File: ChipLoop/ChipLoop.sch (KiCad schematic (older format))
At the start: 33 parts, among them J1 Jumper, J2 Conn_02x25_Counter_Clockwise, Q1 2N3904, SW1 SW_A, SW2 SW_B, U1 ATtiny84A-PU, U2 ISD1820P, U3 L78L05_TO92

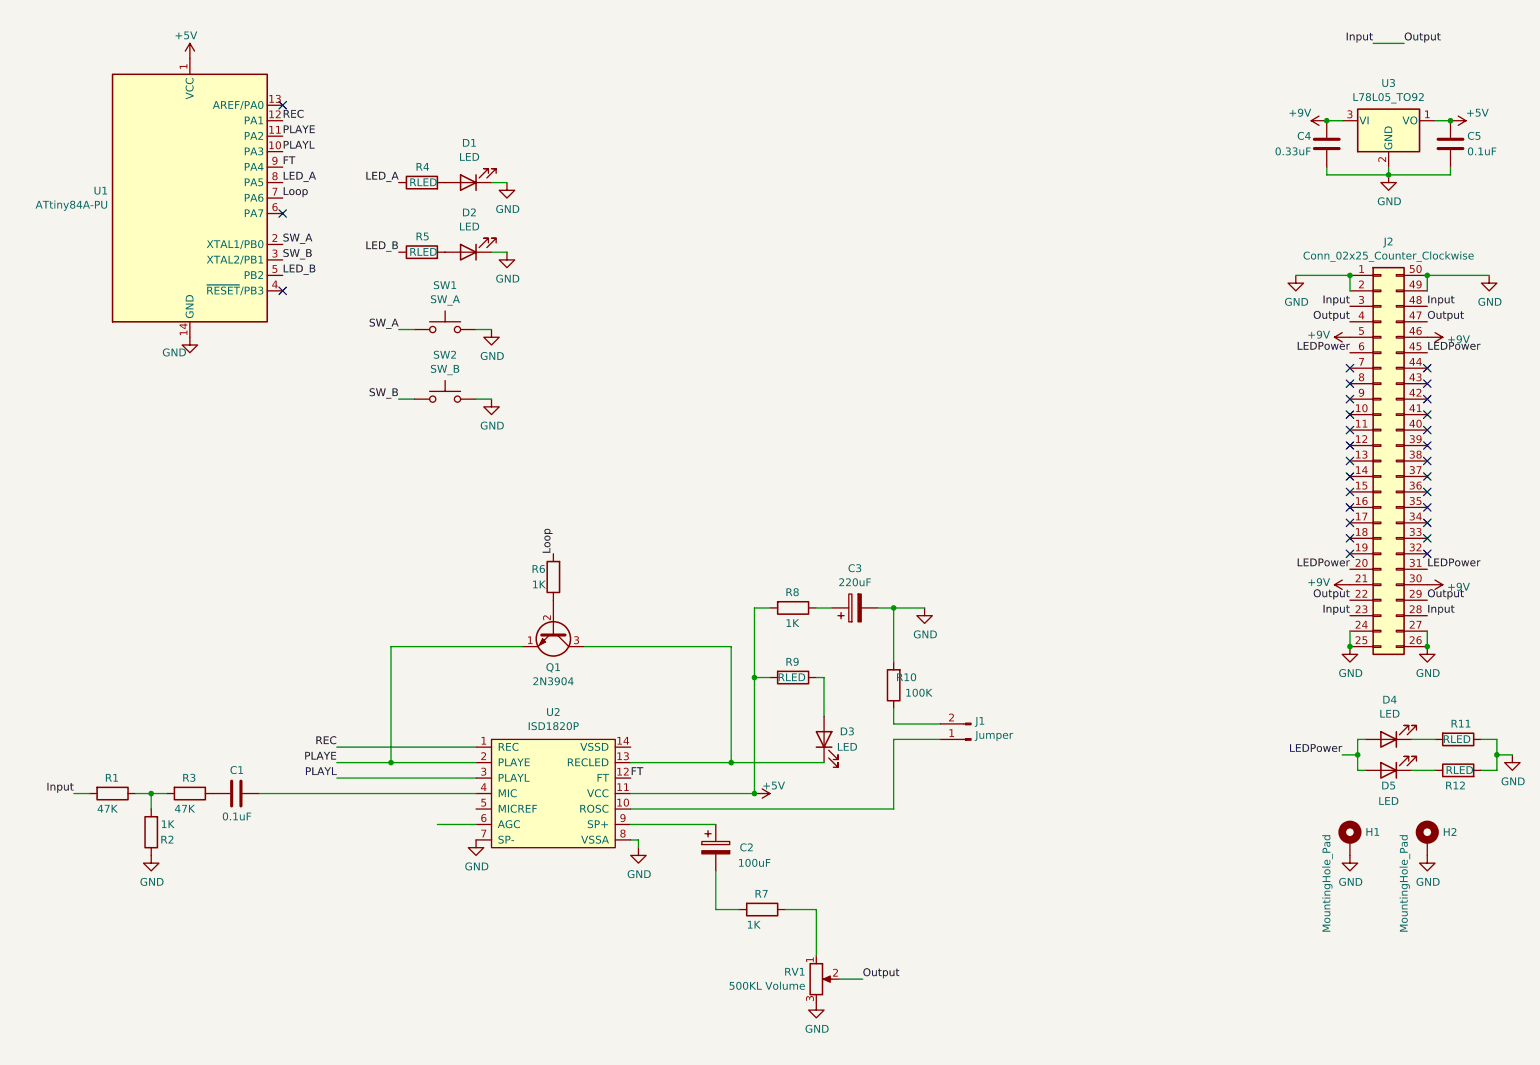
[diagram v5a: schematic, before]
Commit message: Finalized new version of ChipLoop board
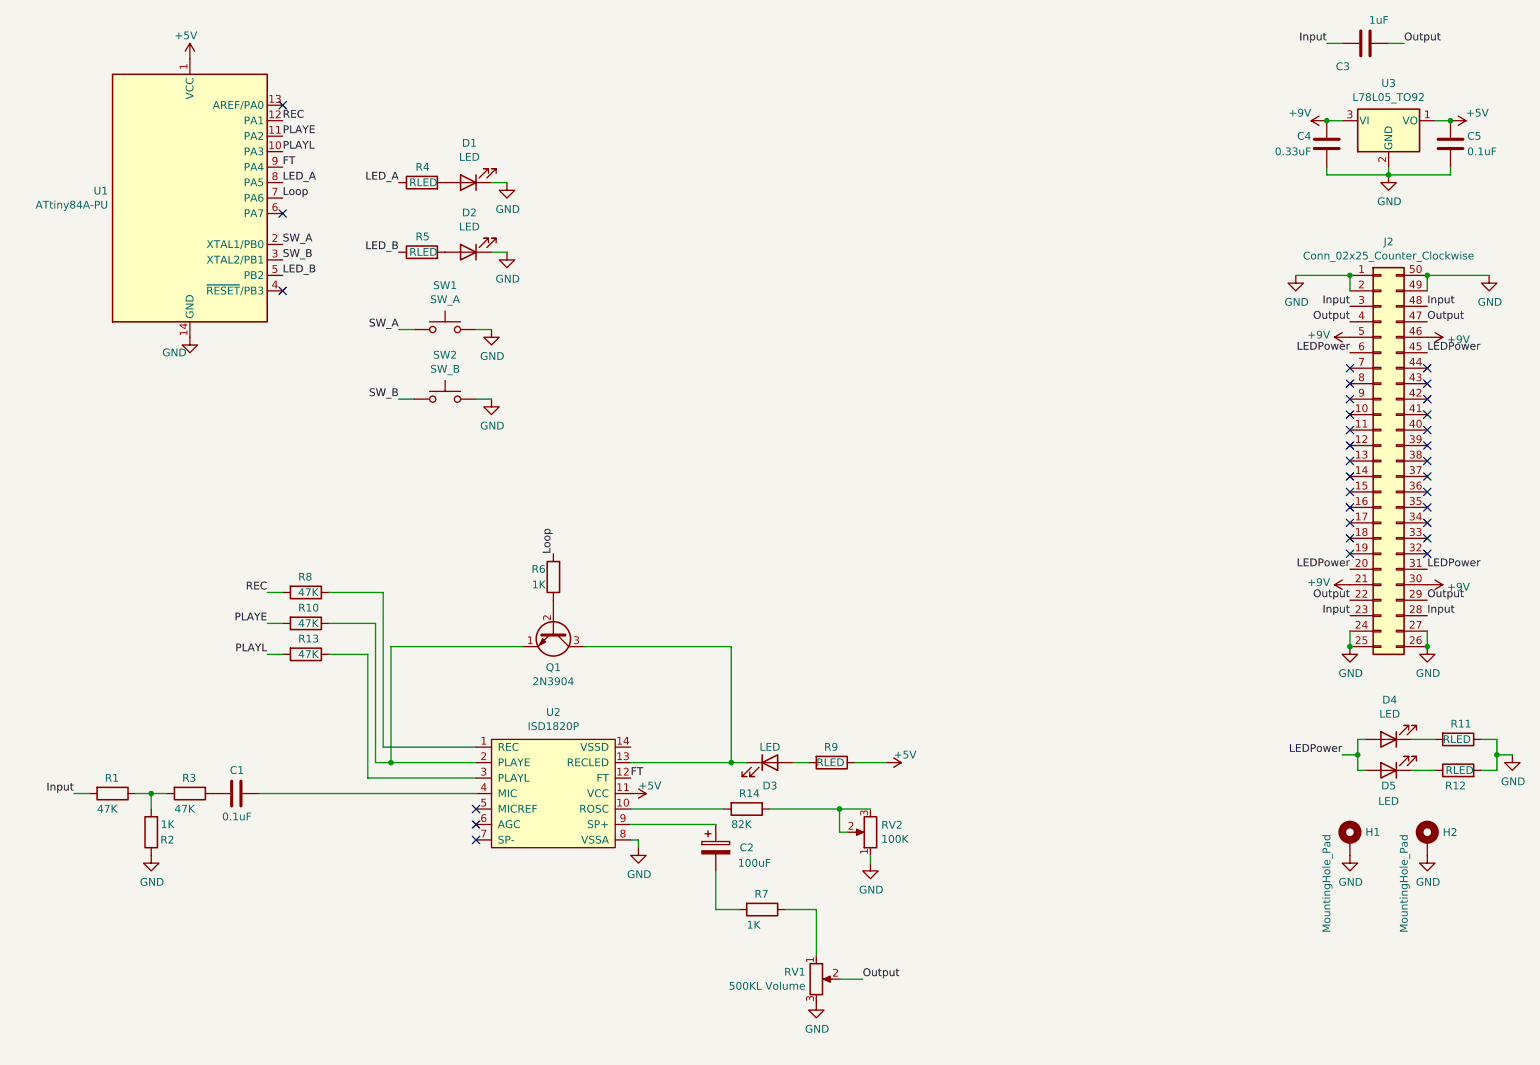
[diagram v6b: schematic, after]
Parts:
- removed C3: 220uF, libraries:CP_Radial_D6.3mm_P2.50mm, symbol Device:CP
- removed J1: Jumper, Connector_PinSocket_2.54mm:PinSocket_1x02_P2.54mm_Vertical, symbol Connector:Conn_01x02_Male
- added C3: 1uF, libraries:C_Flat_L7.2_H10, symbol Device:C
- added R13: 47K, Resistor_THT:R_Axial_DIN0207_L6.3mm_D2.5mm_P10.16mm_Horizontal, symbol Device:R
- added R14: 82K, Resistor_THT:R_Axial_DIN0207_L6.3mm_D2.5mm_P10.16mm_Horizontal, symbol Device:R
- added RV2: 100K, Potentiometer_THT:Potentiometer_Bourns_3386F_Vertical, symbol Device:R_POT
- R10: value 100K -> 47K
- R8: value 1K -> 47K
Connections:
- net +5V: now also R9.1; no longer R8.2, R9.2
- net GND: now also RV2.1; no longer R10.2, U2.7 (SP-)
- net Input: now also C3.1; no longer J2.22 (Pin_22), J2.29 (Pin_29), J2.4 (Pin_4), J2.47 (Pin_47), RV1.2
- net PLAYE: now also R10.2; no longer Q1.1 (E), U2.2 (PLAYE)
- net PLAYL: now also R13.2; no longer U2.3 (PLAYL)
- net REC: now also R8.2; no longer U2.1 (REC)
- net at U2.10 (ROSC): now also R14.2
- net at R8.1: now also U2.1 (REC)
- net at R10.1: now also Q1.1 (E), U2.2 (PLAYE)
- net at D3.2 (A): now also R9.2; no longer R9.1
- new net: R13.1, U2.3 (PLAYL)
- new net: R14.1, RV2.2, RV2.3
- new net Output: C3.2, J2.22 (Pin_22), J2.29 (Pin_29), J2.4 (Pin_4), J2.47 (Pin_47), RV1.2
- no-connect marks 29 -> 32
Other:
- moved on the sheet: D3, R9
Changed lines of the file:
@@
-	1    0    0    -1
-$EndComp
-$Comp
-L power:GND #PWR04
-U 1 1 617CFE57
-P 3400 5900
-F 0 "#PWR04" H 3400 5650 50  0001 C CNN
-F 1 "GND" H 3405 5727 50  0000 C CNN
-F 2 "" H 3400 5900 50  0001 C CNN
-F 3 "" H 3400 5900 50  0001 C CNN
-	1    3400 5900
 	1    0    0    -1
 $EndComp
@@
 Output
 Wire Wire Line
-	3400 5800 3150 5800
-Wire Wire Line
-	3400 5500 2500 5500
-Wire Wire Line
 	3400 5400 2850 5400
-Connection ~ 2850 5400
-Wire Wire Line
-	2850 5400 2500 5400
 $Comp
 L Device:LED D3
 U 1 1 61804FAB
-P 5650 5250
-F 0 "D3" V 5700 5100 50  0000 C CNN
-F 1 "LED" V 5600 5100 50  0000 C CNN
-F 2 "Connector_PinSocket_2.54mm:PinSocket_1x02_P2.54mm_Vertical" H 5650 5250 50  0001 C CNN
-F 3 "~" H 5650 5250 50  0001 C CNN
-	1    5650 5250
-	0    -1   -1   0
+P 5300 5400
+F 0 "D3" H 5300 5250 50  0000 C CNN
+F 1 "LED" H 5300 5500 50  0000 C CNN
+F 2 "Connector_PinSocket_2.54mm:PinSocket_1x02_P2.54mm_Vertical" H 5300 5400 50  0001 C CNN
+F 3 "~" H 5300 5400 50  0001 C CNN
+	1    5300 5400
+	1    0    0    -1
 $EndComp
 Wire Wire Line
 	5050 5400 4400 5400
-Wire Wire Line
-	5650 5400 5050 5400
-Connection ~ 5050 5400
 $Comp
 L Device:R R9
 U 1 1 6181485B
-P 5450 4850
-F 0 "R9" V 5350 4800 50  0000 L CNN
-F 1 "RLED" V 5450 4750 50  0000 L CNN
-F 2 "Resistor_THT:R_Axial_DIN0207_L6.3mm_D2.5mm_P10.16mm_Horizontal" V 5380 4850 50  0001 C CNN
-F 3 "~" H 5450 4850 50  0001 C CNN
-	1    5450 4850
-	0    1    1    0
-$EndComp
-Wire Wire Line
-	5600 4850 5650 4850
-Wire Wire Line
-	5650 4850 5650 5100
-Wire Wire Line
-	5300 4850 5200 4850
-Wire Wire Line
-	5200 4850 5200 5600
-Wire Wire Line
-	5200 5600 4400 5600
-Connection ~ 5200 5600
+P 5700 5400
+F 0 "R9" V 5600 5350 50  0000 L CNN
+F 1 "RLED" V 5700 5300 50  0000 L CNN
+F 2 "Resistor_THT:R_Axial_DIN0207_L6.3mm_D2.5mm_P10.16mm_Horizontal" V 5630 5400 50  0001 C CNN
+F 3 "~" H 5700 5400 50  0001 C CNN
+	1    5700 5400
+	0    1    1    0
+$EndComp
 $Comp
 L MCU_Microchip_ATtiny:ATtiny84A-PU U1
@@
 	1    0    0    -1
 $EndComp
-Text Label 2500 5300 2    50   ~ 0
+Text Label 2050 4300 2    50   ~ 0
 REC
-Text Label 2500 5400 2    50   ~ 0
+Text Label 2050 4500 2    50   ~ 0
 PLAYE
-Text Label 2500 5500 2    50   ~ 0
+Text Label 2050 4700 2    50   ~ 0
 PLAYL
 Text Label 2150 1250 0    50   ~ 0
@@
 FT
 $Comp
-L Device:R R8
-U 1 1 617D2BF7
-P 5450 4400
-F 0 "R8" V 5350 4350 50  0000 L CNN
-F 1 "1K" V 5550 4350 50  0000 L CNN
-F 2 "Resistor_THT:R_Axial_DIN0207_L6.3mm_D2.5mm_P10.16mm_Horizontal" V 5380 4400 50  0001 C CNN
-F 3 "~" H 5450 4400 50  0001 C CNN
-	1    5450 4400
-	0    1    1    0
-$EndComp
-Connection ~ 5200 4850
-Wire Wire Line
-	5200 4400 5300 4400
-Wire Wire Line
-	5200 4400 5200 4850
-$Comp
-L Device:CP C3
-U 1 1 617E3B4B
-P 5850 4400
-F 0 "C3" V 6105 4400 50  0000 C CNN
-F 1 "220uF" V 6014 4400 50  0000 C CNN
-F 2 "libraries:CP_Radial_D6.3mm_P2.50mm" H 5888 4250 50  0001 C CNN
-F 3 "~" H 5850 4400 50  0001 C CNN
-	1    5850 4400
-	0    -1   -1   0
-$EndComp
-$Comp
-L power:GND #PWR012
-U 1 1 617E5A61
-P 6300 4400
-F 0 "#PWR012" H 6300 4150 50  0001 C CNN
-F 1 "GND" H 6305 4227 50  0000 C CNN
-F 2 "" H 6300 4400 50  0001 C CNN
-F 3 "" H 6300 4400 50  0001 C CNN
-	1    6300 4400
-	1    0    0    -1
-$EndComp
-Wire Wire Line
-	6300 4400 6100 4400
-$Comp
-L Device:R R10
-U 1 1 617E9A9D
-P 6100 4900
-F 0 "R10" H 5950 4850 50  0000 L CNN
-F 1 "100K" H 5850 4950 50  0000 L CNN
-F 2 "Resistor_THT:R_Axial_DIN0207_L6.3mm_D2.5mm_P10.16mm_Horizontal" V 6030 4900 50  0001 C CNN
-F 3 "~" H 6100 4900 50  0001 C CNN
-	1    6100 4900
-	-1   0    0    1
-$EndComp
-Wire Wire Line
-	6100 4750 6100 4400
-Connection ~ 6100 4400
-Wire Wire Line
-	6100 4400 6000 4400
-Wire Wire Line
-	6100 5700 4400 5700
-$Comp
 L power:+5V #PWR02
 U 1 1 61800A49
@@
 L power:+5V #PWR010
 U 1 1 6180A81B
-P 5200 5600
-F 0 "#PWR010" H 5200 5450 50  0001 C CNN
-F 1 "+5V" V 5150 5650 50  0000 L CNN
-F 2 "" H 5200 5600 50  0001 C CNN
-F 3 "" H 5200 5600 50  0001 C CNN
-	1    5200 5600
+P 6050 5400
+F 0 "#PWR010" H 6050 5250 50  0001 C CNN
+F 1 "+5V" V 6000 5450 50  0000 L CNN
+F 2 "" H 6050 5400 50  0001 C CNN
+F 3 "" H 6050 5400 50  0001 C CNN
+	1    6050 5400
 	0    1    1    0
 $EndComp
@@
 	1    0    0    -1
 $EndComp
-Text Label 9200 750  2    50   ~ 0
+Text Label 8900 750  2    50   ~ 0
 Input
 Text Label 9400 750  0    50   ~ 0
 Output
-Wire Wire Line
-	9400 750  9200 750
 Text Label 800  5600 2    50   ~ 0
 Input
@@
 Wire Wire Line
 	2000 5600 3400 5600
-Wire Wire Line
-	5600 4400 5700 4400
-Wire Wire Line
-	2500 5300 3400 5300
 $Comp
 L power:GND #PWR09
@@
 Wire Wire Line
 	4450 5900 4400 5900
-Wire Wire Line
-	6100 5250 6100 5700
-Wire Wire Line
-	6100 5150 6100 5050
-Wire Wire Line
-	6400 5150 6100 5150
-Wire Wire Line
-	6400 5250 6100 5250
-$Comp
-L Connector:Conn_01x02_Male J1
-U 1 1 617ECA40
-P 6600 5250
-F 0 "J1" H 6572 5132 50  0000 R CNN
-F 1 "Jumper" H 6572 5223 50  0000 R CNN
-F 2 "Connector_PinSocket_2.54mm:PinSocket_1x02_P2.54mm_Vertical" H 6600 5250 50  0001 C CNN
-F 3 "~" H 6600 5250 50  0001 C CNN
-	1    6600 5250
-	-1   0    0    1
-$EndComp
 $Comp
 L Device:CP C2
@@
 Wire Wire Line
 	5400 6350 5600 6350
+$Comp
+L Device:R R8
+U 1 1 621D81C1
+P 2300 4300
+F 0 "R8" V 2200 4250 50  0000 L CNN
+F 1 "47K" V 2300 4250 50  0000 L CNN
+F 2 "Resistor_THT:R_Axial_DIN0207_L6.3mm_D2.5mm_P10.16mm_Horizontal" V 2230 4300 50  0001 C CNN
+F 3 "~" H 2300 4300 50  0001 C CNN
+	1    2300 4300
+	0    1    1    0
+$EndComp
+Wire Wire Line
+	2050 4300 2150 4300
+$Comp
+L Device:R R10
+U 1 1 621DDB9D
+P 2300 4500
+F 0 "R10" V 2200 4450 50  0000 L CNN
+F 1 "47K" V 2300 4450 50  0000 L CNN
+F 2 "Resistor_THT:R_Axial_DIN0207_L6.3mm_D2.5mm_P10.16mm_Horizontal" V 2230 4500 50  0001 C CNN
+F 3 "~" H 2300 4500 50  0001 C CNN
+	1    2300 4500
+	0    1    1    0
+$EndComp
+$Comp
+L Device:R R13
+U 1 1 621E1B15
+P 2300 4700
+F 0 "R13" V 2200 4650 50  0000 L CNN
+F 1 "47K" V 2300 4650 50  0000 L CNN
+F 2 "Resistor_THT:R_Axial_DIN0207_L6.3mm_D2.5mm_P10.16mm_Horizontal" V 2230 4700 50  0001 C CNN
+F 3 "~" H 2300 4700 50  0001 C CNN
+	1    2300 4700
+	0    1    1    0
+$EndComp
+Wire Wire Line
+	2050 4500 2150 4500
+Wire Wire Line
+	2050 4700 2150 4700
+Wire Wire Line
+	2450 4300 2800 4300
+Wire Wire Line
+	2800 4300 2800 5300
+Wire Wire Line
+	2800 5300 3400 5300
+Wire Wire Line
+	2850 5400 2750 5400
+Wire Wire Line
+	2750 5400 2750 4500
+Wire Wire Line
+	2750 4500 2450 4500
+Connection ~ 2850 5400
+Wire Wire Line
+	3400 5500 2700 5500
+Wire Wire Line
+	2700 5500 2700 4700
+Wire Wire Line
+	2700 4700 2450 4700
+NoConn ~ 3400 5700
+NoConn ~ 3400 5800
+NoConn ~ 3400 5900
+$Comp
+L power:+5V #PWR04
+U 1 1 621FA75D
+P 4400 5600
+F 0 "#PWR04" H 4400 5450 50  0001 C CNN
+F 1 "+5V" V 4350 5650 50  0000 L CNN
+F 2 "" H 4400 5600 50  0001 C CNN
+F 3 "" H 4400 5600 50  0001 C CNN
+	1    4400 5600
+	0    1    1    0
+$EndComp
+Wire Wire Line
+	5150 5400 5050 5400
+Connection ~ 5050 5400
+Wire Wire Line
+	5550 5400 5450 5400
+$Comp
+L power:GND #PWR012
+U 1 1 6220886F
+P 5950 6050
+F 0 "#PWR012" H 5950 5800 50  0001 C CNN
+F 1 "GND" H 5955 5877 50  0000 C CNN
+F 2 "" H 5950 6050 50  0001 C CNN
+F 3 "" H 5950 6050 50  0001 C CNN
+	1    5950 6050
+	1    0    0    -1
+$EndComp
+$Comp
+L Device:C C3
+U 1 1 62209A7E
+P 9150 750
+F 0 "C3" V 9000 850 50  0000 L CNN
+F 1 "1uF" V 9300 600 50  0000 L CNN
+F 2 "libraries:C_Flat_L7.2_H10" H 9188 600 50  0001 C CNN
+F 3 "~" H 9150 750 50  0001 C CNN
+	1    9150 750
+	0    -1   -1   0
+$EndComp
+Wire Wire Line
+	9400 750  9300 750
+Wire Wire Line
+	9000 750  8900 750
+Wire Wire Line
+	5850 5400 6050 5400
+$Comp
+L Device:R R14
+U 1 1 6220E5E9
+P 5150 5700
+F 0 "R14" V 5050 5650 50  0000 L CNN
+F 1 "82K" V 5250 5600 50  0000 L CNN
+F 2 "Resistor_THT:R_Axial_DIN0207_L6.3mm_D2.5mm_P10.16mm_Horizontal" V 5080 5700 50  0001 C CNN
+F 3 "~" H 5150 5700 50  0001 C CNN
+	1    5150 5700
+	0    1    1    0
+$EndComp
+Wire Wire Line
+	5000 5700 4400 5700
+$Comp
+L Device:R_POT RV2
+U 1 1 62210FD6
+P 5950 5850
+F 0 "RV2" H 5880 5804 50  0000 R CNN
+F 1 "100K" H 5880 5895 50  0000 R CNN
+F 2 "Potentiometer_THT:Potentiometer_Bourns_3386F_Vertical" H 5950 5850 50  0001 C CNN
+F 3 "~" H 5950 5850 50  0001 C CNN
+	1    5950 5850
+	-1   0    0    1
+$EndComp
+Wire Wire Line
+	5950 6050 5950 6000
+Wire Wire Line
+	5950 5700 5750 5700
+Wire Wire Line
+	5750 5700 5750 5850
+Wire Wire Line
+	5750 5850 5800 5850
+Wire Wire Line
+	5300 5700 5750 5700
+Connection ~ 5750 5700
 $EndSCHEMATC
